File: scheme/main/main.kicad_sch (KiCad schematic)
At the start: 4 parts, among them U1 ACS712xLCTR-05B, U2 ACS712xLCTR-05B, U3 ACS712xLCTR-05B

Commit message: itrip circuit
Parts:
- removed IPM1: ~, main:IC_IKCM30F60GDXKMA1, symbol main:IGCM06F60GA
- removed U1, U2, U3: ACS712xLCTR-05B, Package_SO:SOIC-8_3.9x4.9mm_P1.27mm, symbol Sensor_Current:ACS712xLCTR-05B
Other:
- added sheet Current Filter U (current_filter.kicad_sch)
- added sheet Current Filter V (current_filter.kicad_sch)
- added sheet Current Filter W (current_filter.kicad_sch)
- added sheet Current Sense U (current_sense.kicad_sch)
- added sheet Current Sense V (current_sense.kicad_sch)
- added sheet Current Sense W (current_sense.kicad_sch)
- added sheet IPM (ipm.kicad_sch)

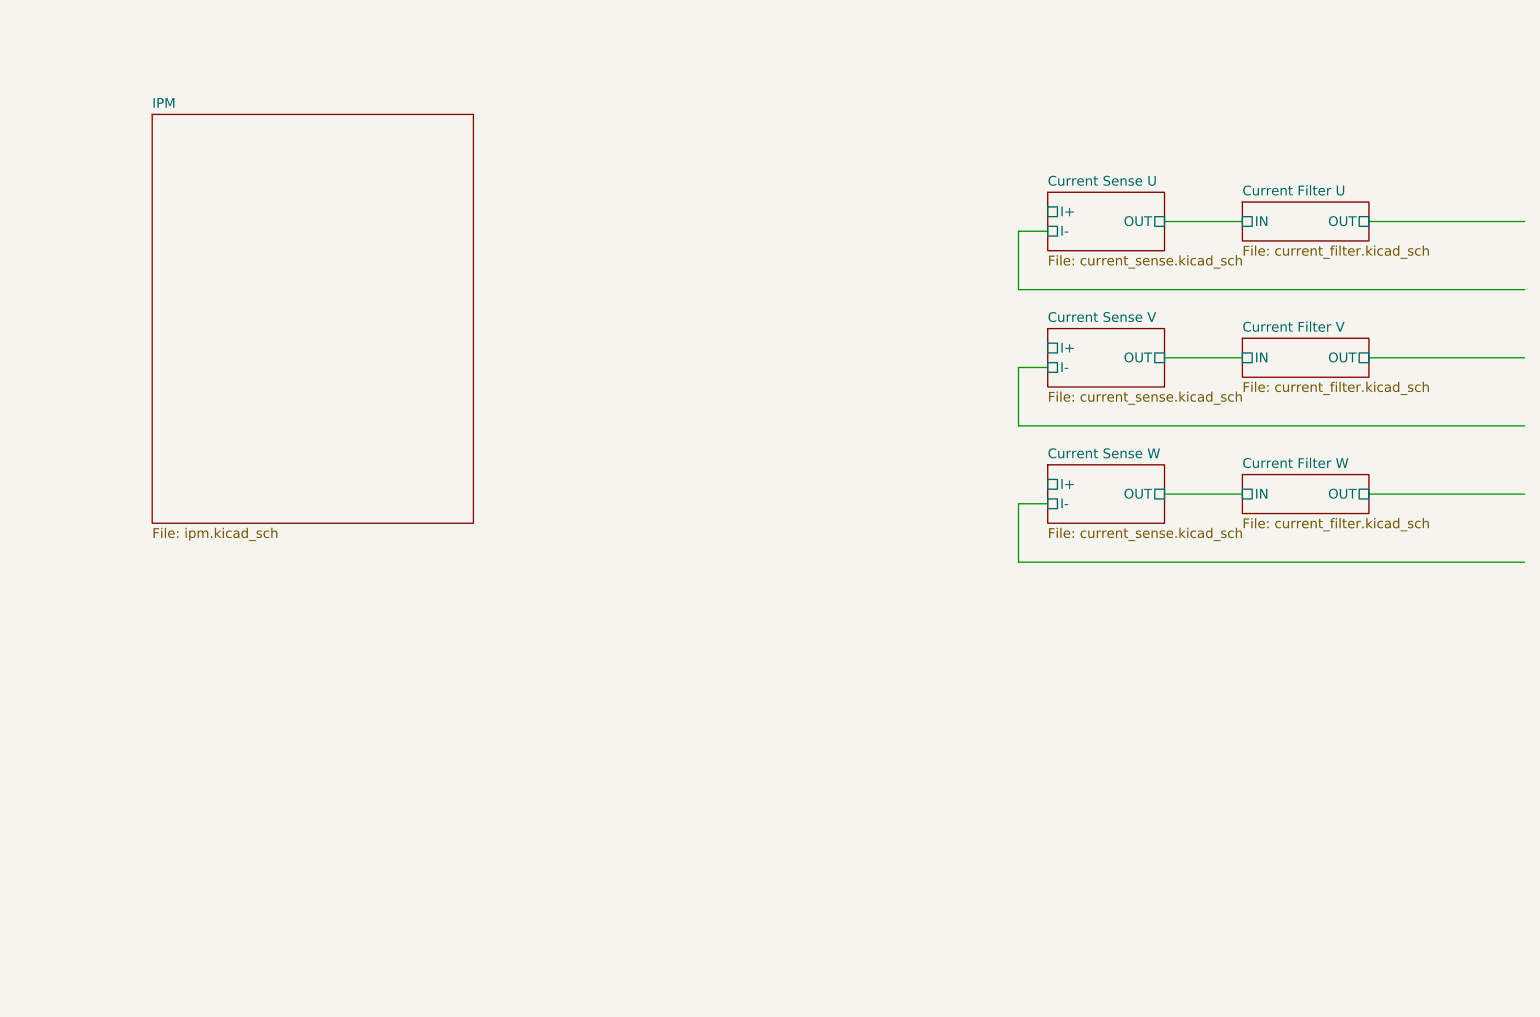
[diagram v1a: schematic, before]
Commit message: bootstrap dc-dc add capacitors & more
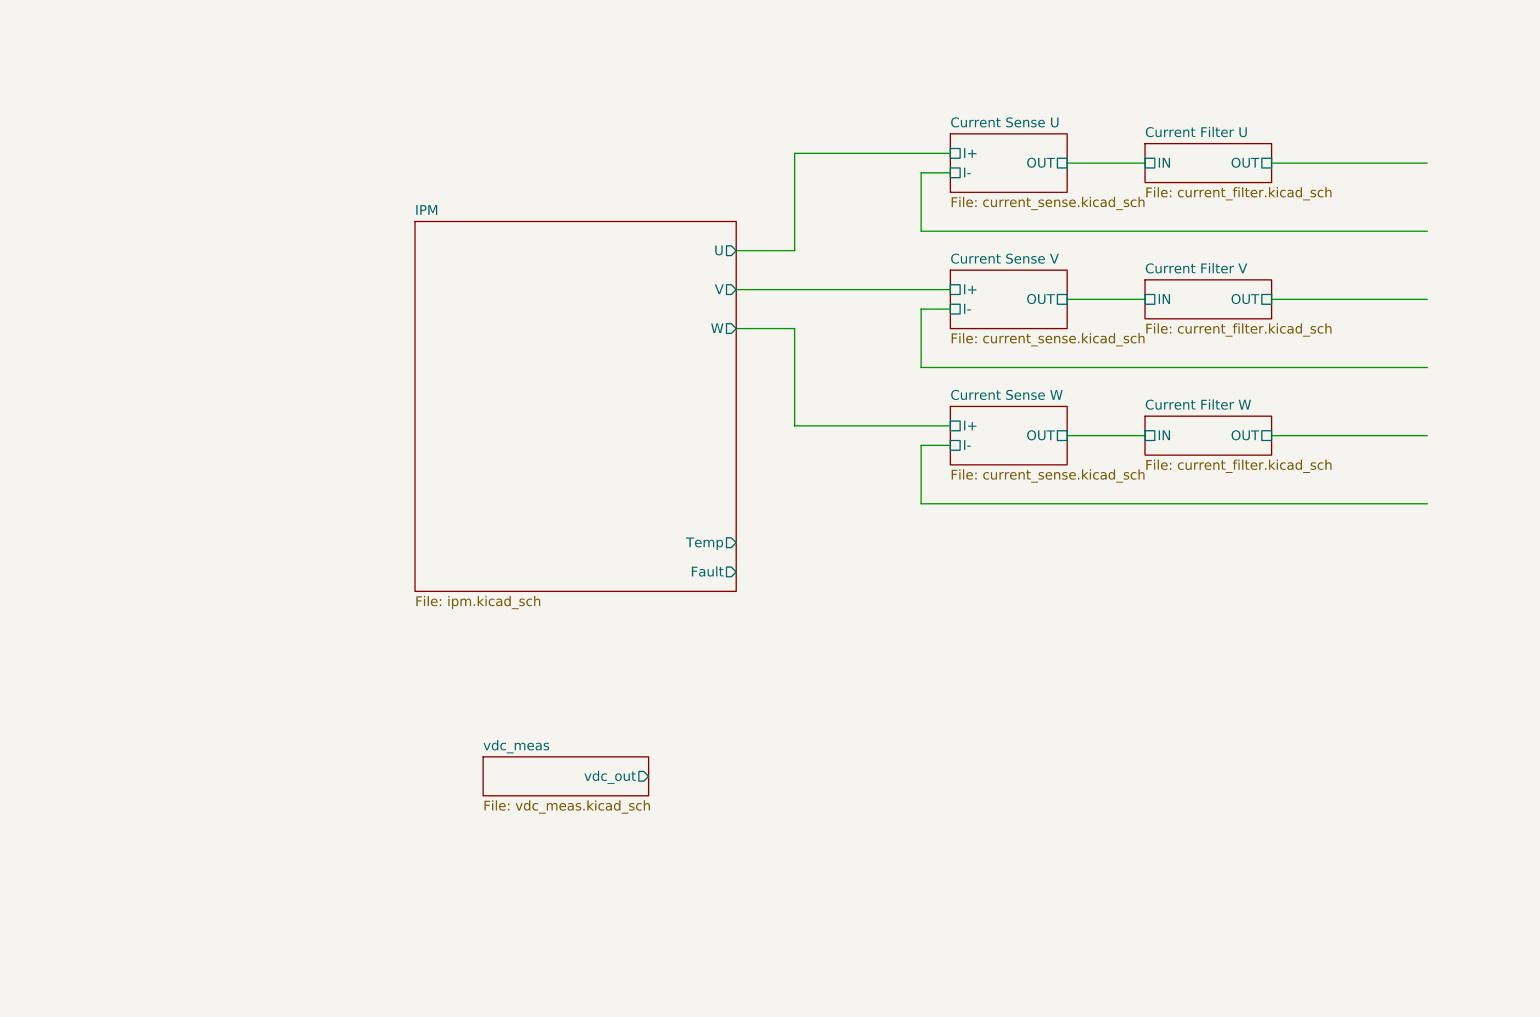
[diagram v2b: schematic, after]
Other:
- added sheet vdc_meas (vdc_meas.kicad_sch)
- sheet IPM ports: added Fault, Temp, U, V, W; removed none

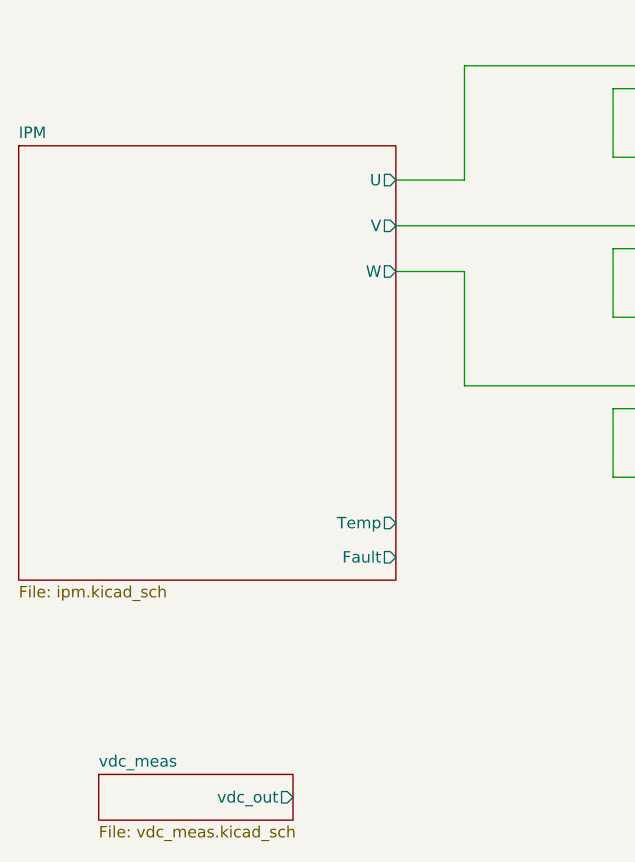
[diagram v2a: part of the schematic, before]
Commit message: control isolation schematic
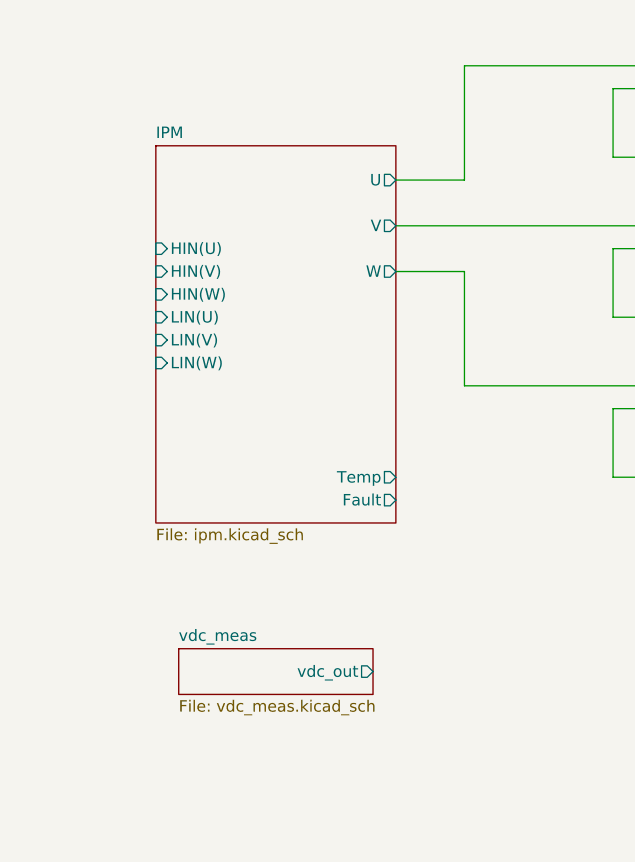
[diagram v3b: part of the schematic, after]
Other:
- sheet IPM ports: added HIN(U), HIN(V), HIN(W), LIN(U), LIN(V), LIN(W); removed none
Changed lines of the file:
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@@
 	)
 	(sheet
-		(at 128.27 59.69)
-		(size 41.91 48.26)
+		(at 143.51 59.69)
+		(size 26.67 41.91)
 		(fields_autoplaced yes)
 		(stroke
@@
 		)
 		(property "Sheetname" "IPM"
-			(at 128.27 58.9784 0)
+			(at 143.51 58.9784 0)
 			(effects
 				(font
@@
 		)
 		(property "Sheetfile" "ipm.kicad_sch"
-			(at 128.27 108.5346 0)
+			(at 143.51 102.1846 0)
 			(effects
 				(font
@@
 		)
 		(pin "Temp" output
-			(at 170.18 101.6 0)
+			(at 170.18 96.52 0)
 			(effects
 				(font
@@
 		)
 		(pin "Fault" output
-			(at 170.18 105.41 0)
-			(effects
-				(font
-					(size 1.27 1.27)
-				)
-				(justify right)
+			(at 170.18 99.06 0)
+			(effects
+				(font
+					(size 1.27 1.27)
+				)
+				(justify right)
+			)
+		)
+		(pin "HIN(W)" input
+			(at 143.51 76.2 180)
+			(effects
+				(font
+					(size 1.27 1.27)
+				)
+				(justify left)
+			)
+		)
+		(pin "LIN(W)" input
+			(at 143.51 83.82 180)
+			(effects
+				(font
+					(size 1.27 1.27)
+				)
+				(justify left)
+			)
+		)
+		(pin "HIN(V)" input
+			(at 143.51 73.66 180)
+			(effects
+				(font
+					(size 1.27 1.27)
+				)
+				(justify left)
+			)
+		)
+		(pin "LIN(V)" input
+			(at 143.51 81.28 180)
+			(effects
+				(font
+					(size 1.27 1.27)
+				)
+				(justify left)
+			)
+		)
+		(pin "LIN(U)" input
+			(at 143.51 78.74 180)
+			(effects
+				(font
+					(size 1.27 1.27)
+				)
+				(justify left)
+			)
+		)
+		(pin "HIN(U)" input
+			(at 143.51 71.12 180)
+			(effects
+				(font
+					(size 1.27 1.27)
+				)
+				(justify left)
 			)
 		)
@@
 	)
 	(sheet
-		(at 137.16 129.54)
+		(at 146.05 115.57)
 		(size 21.59 5.08)
 		(fields_autoplaced yes)
@@
 		)
 		(property "Sheetname" "vdc_meas"
-			(at 137.16 128.8284 0)
+			(at 146.05 114.8584 0)
 			(effects
 				(font
@@
 		)
 		(property "Sheetfile" "vdc_meas.kicad_sch"
-			(at 137.16 135.2046 0)
+			(at 146.05 121.2346 0)
 			(effects
 				(font
@@
 		)
 		(pin "vdc_out" output
-			(at 158.75 132.08 0)
+			(at 167.64 118.11 0)
 			(effects
 				(font
@@
 			(project "main"
 				(path "/c11d1dbc-4db9-4712-8d1d-5f6f7086cded"
-					(page "6")
+					(page "5")
 				)
 			)
@@
 			(project "main"
 				(path "/c11d1dbc-4db9-4712-8d1d-5f6f7086cded"
-					(page "5")
-				)
-			)
+					(page "6")
+				)
+			)

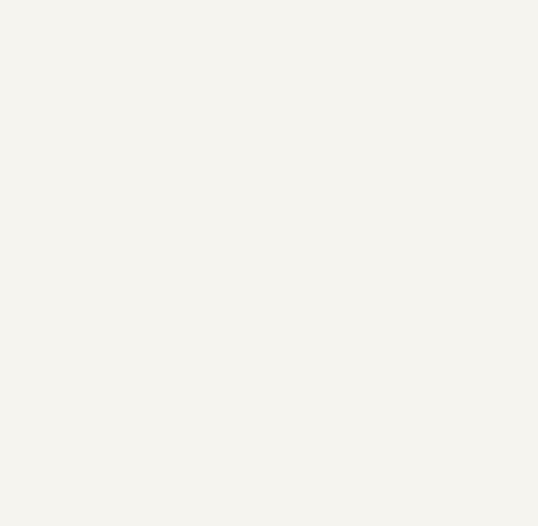
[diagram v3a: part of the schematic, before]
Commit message: power scheme in progress (added dc-dc)
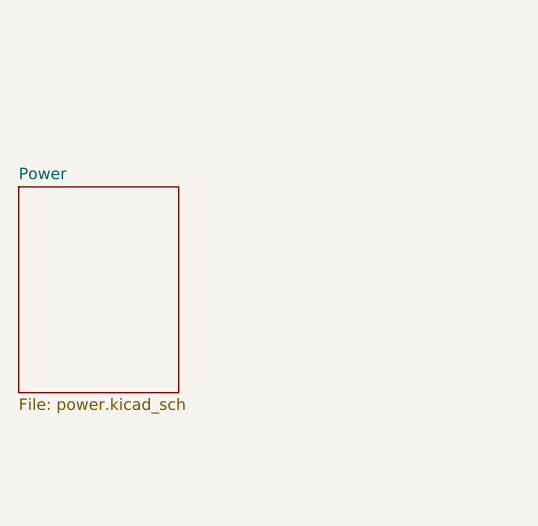
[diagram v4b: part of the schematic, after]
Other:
- added sheet Power (power.kicad_sch)
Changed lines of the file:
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@@
+		)
+	)
+	(sheet
+		(at 85.09 87.63)
+		(size 17.78 22.86)
+		(fields_autoplaced yes)
+		(stroke
+			(width 0.1524)
+			(type solid)
+		)
+		(fill
+			(color 255 255 194 1.0000)
+		)
+		(property "Sheetname" "Power"
+			(at 85.09 86.9184 0)
+			(effects
+				(font
+					(size 1.27 1.27)
+				)
+				(justify left bottom)
+			)
+		)
+		(property "Sheetfile" "power.kicad_sch"
+			(at 85.09 111.0746 0)
+			(effects
+				(font
+					(size 1.27 1.27)
+				)
+				(justify left top)
+			)
+		)
+		(instances
+			(project "main"
+				(path "/c11d1dbc-4db9-4712-8d1d-5f6f7086cded"
+					(page "16")
+				)
+			)
 		)
 	)

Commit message: power scheme
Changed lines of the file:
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@@
 	)
 	(sheet
-		(at 85.09 87.63)
-		(size 17.78 22.86)
+		(at 146.05 133.35)
+		(size 22.86 25.4)
 		(fields_autoplaced yes)
 		(stroke
@@
 		)
 		(property "Sheetname" "Power"
-			(at 85.09 86.9184 0)
+			(at 146.05 132.6384 0)
 			(effects
 				(font
@@
 		)
 		(property "Sheetfile" "power.kicad_sch"
-			(at 85.09 111.0746 0)
+			(at 146.05 159.3346 0)
 			(effects
 				(font

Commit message: separate hi power & signal gnd
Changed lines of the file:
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@@
 	(sheet
 		(at 146.05 133.35)
-		(size 22.86 25.4)
+		(size 22.86 5.08)
 		(fields_autoplaced yes)
 		(stroke
@@
 		)
 		(property "Sheetfile" "power.kicad_sch"
-			(at 146.05 159.3346 0)
+			(at 146.05 139.0146 0)
 			(effects
 				(font

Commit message: vdc scheme
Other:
- added sheet Rectifier_dc (rectifier_dc.kicad_sch)
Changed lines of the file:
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@@
+	)
+	(sheet
+		(at 76.2 71.12)
+		(size 25.4 31.75)
+		(fields_autoplaced yes)
+		(stroke
+			(width 0.1524)
+			(type solid)
+		)
+		(fill
+			(color 255 255 194 1.0000)
+		)
+		(property "Sheetname" "Rectifier_dc"
+			(at 76.2 70.4084 0)
+			(effects
+				(font
+					(size 1.27 1.27)
+				)
+				(justify left bottom)
+			)
+		)
+		(property "Sheetfile" "rectifier_dc.kicad_sch"
+			(at 76.2 103.4546 0)
+			(effects
+				(font
+					(size 1.27 1.27)
+				)
+				(justify left top)
+			)
+		)
+		(instances
+			(project "main"
+				(path "/c11d1dbc-4db9-4712-8d1d-5f6f7086cded"
+					(page "17")
+				)
+			)
+		)
 	)
 	(sheet

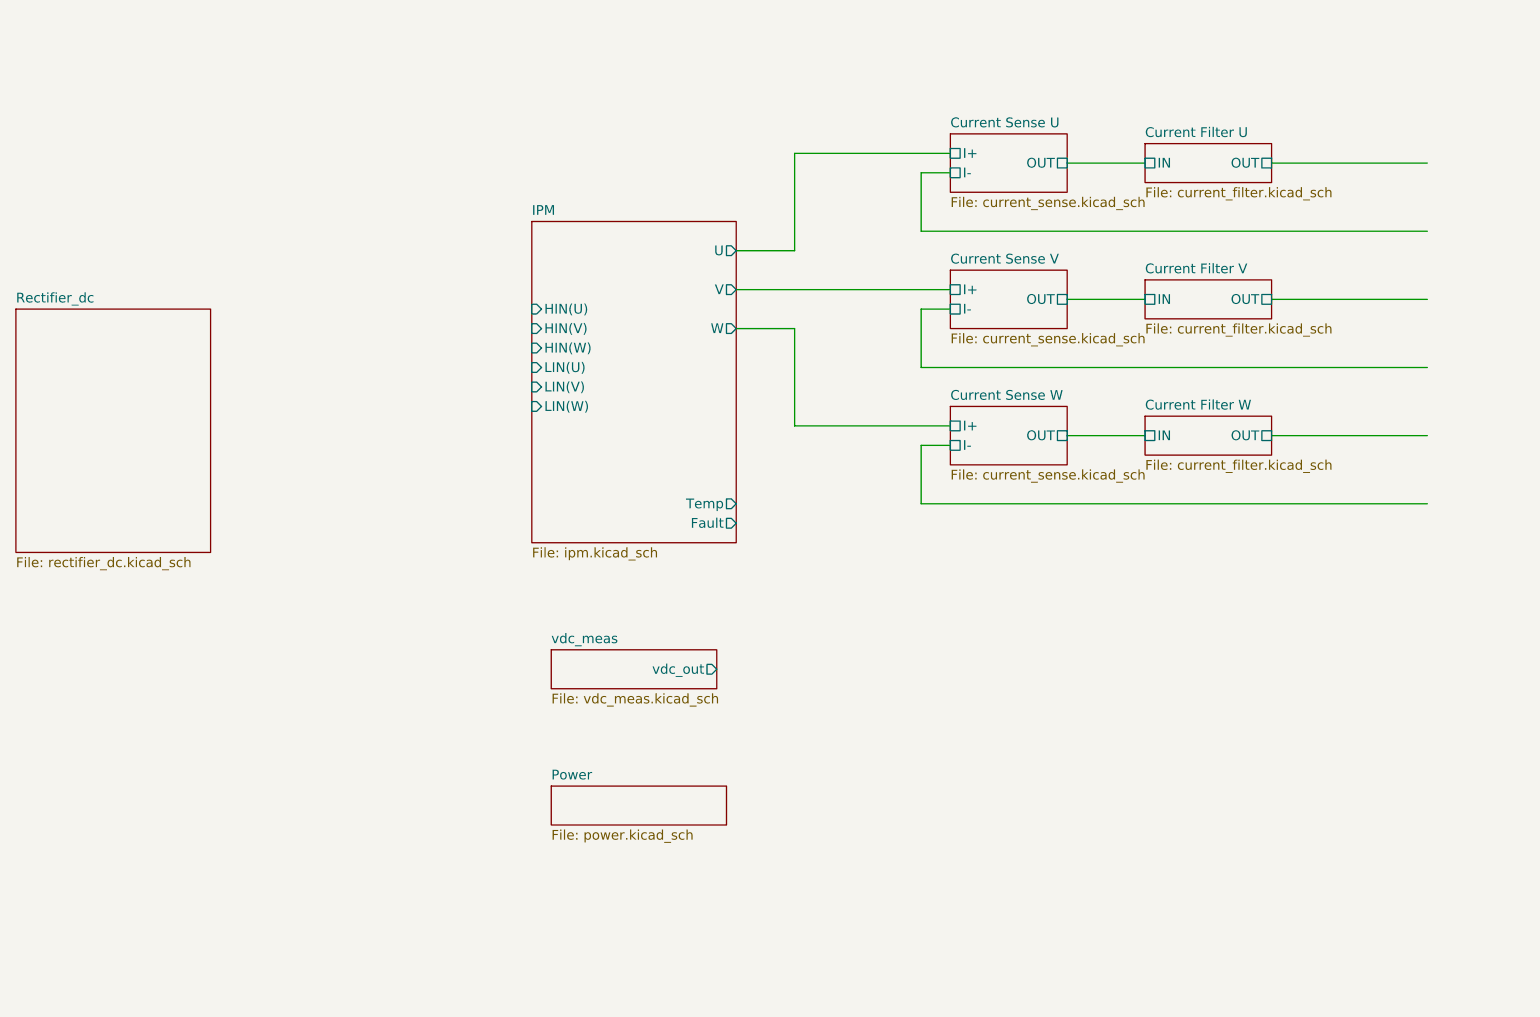
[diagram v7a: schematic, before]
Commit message: added ac/dc 24V
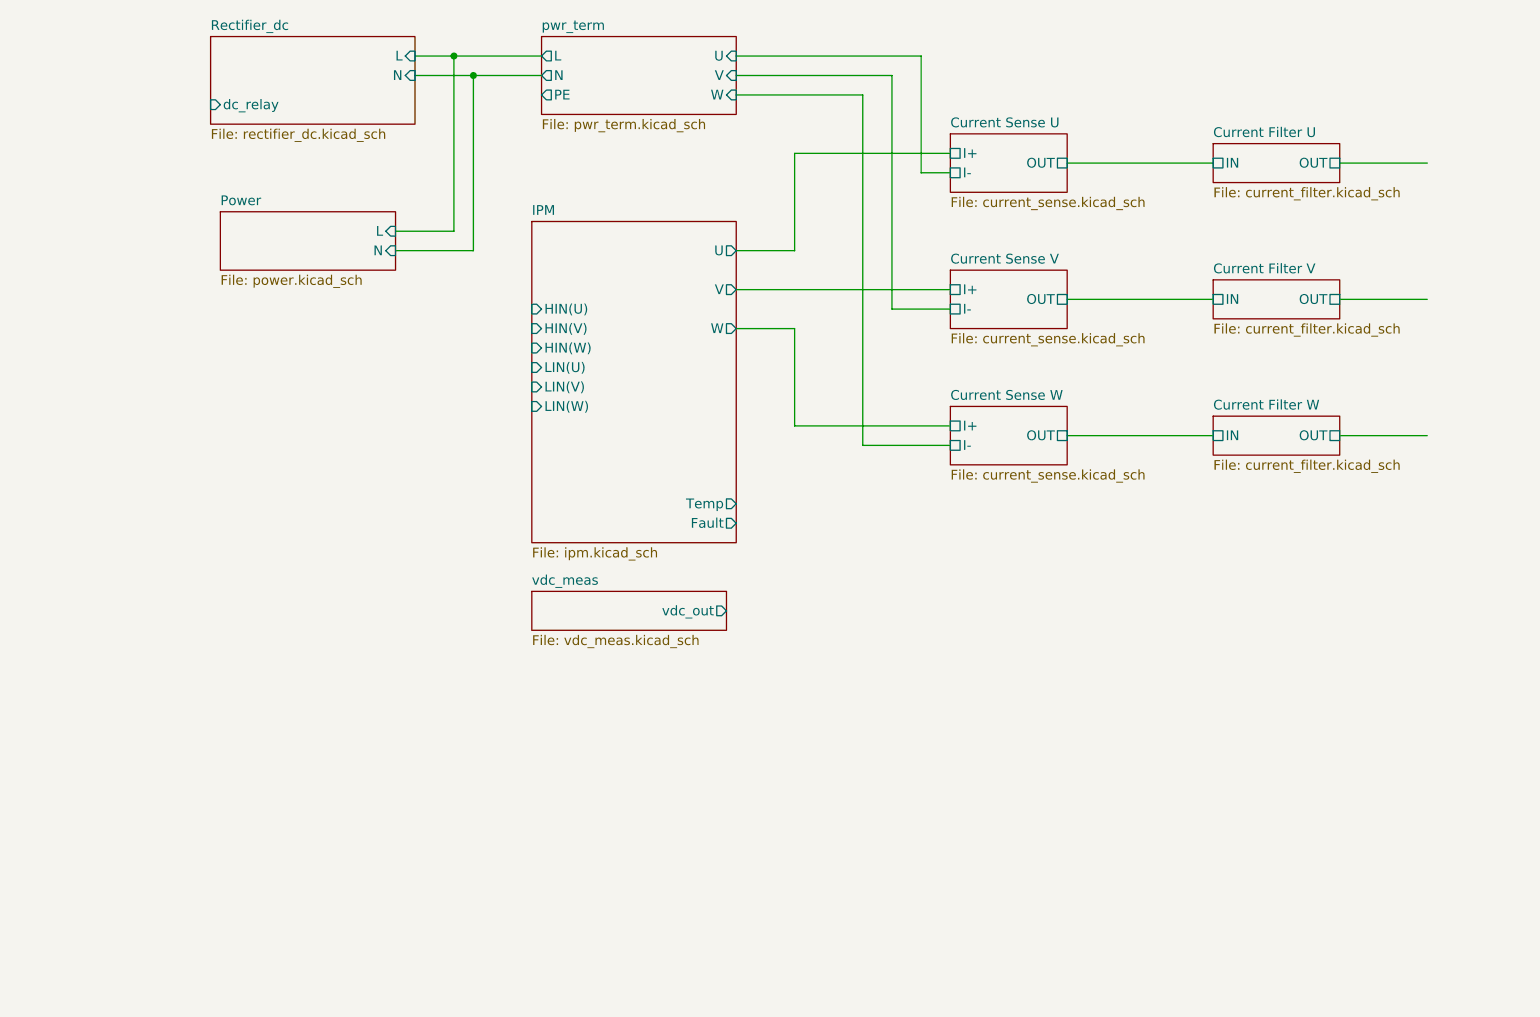
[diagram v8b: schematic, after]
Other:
- added sheet pwr_term (pwr_term.kicad_sch)
- sheet Power ports: added L, N; removed none
- sheet Rectifier_dc ports: added L, N, dc_relay; removed none
